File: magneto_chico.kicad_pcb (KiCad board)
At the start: 2 copper layers, 53 parts, among them P1 CONN_01X02, P2 CONN_01X01, P3 CONN_01X01, P4 CONN_01X01, P5 CONN_5, P6 CONN_01X04, Q1 BC817-40, Q2 BC817-40, Q3 BC817-40, Q4 BC807-40, Q5 IRF540, Q6 BC817-40, SW1 SPST, U1 78L33, U2 STM32F030K6, U3 LM358

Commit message: empiezo a rutear
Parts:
- C1: footprint LOCAL_Connectors_Molex:Molex_KK_6410-03 -> LOCAL_Capacitors_ThroughHole:C_Radial_D10_L20_P5
- C5, C6, C7, Q1, Q2, Q3, Q4, Q6, R1, R10, R11, R12, R13, R14, R15, R16, R17, R2, R20, R3, R4, R5, R6, R7, R8, R9, U2, U3: moved to B.Cu
- SP1: footprint LOCAL_Pin_Headers:Pin_Header_Straight_1x02 -> LOCAL_Capacitors_ThroughHole:C_Radial_D10_L20_P5
- moved R2 121.9 mm to (115.6, 72.4), turned to 270 degrees
- moved Q1 121.2 mm to (112.5, 72.4), turned to 180 degrees
- moved P1 119.8 mm to (103.1, 65.3), turned to 180 degrees
- moved C4 119.0 mm to (127.8, 65.0), turned to 90 degrees
- moved U1 116.8 mm to (103.4, 80.5), turned to 90 degrees
- moved R1 112.8 mm to (119.9, 80.5), turned to 90 degrees
- moved C3 111.8 mm to (108.7, 81.8), turned to 90 degrees
- moved C1 108.3 mm to (115.8, 68.1), turned to 90 degrees
- moved P3 107.5 mm to (114.3, 81.8)
- moved C2 104.4 mm to (103.1, 91.7), turned to 180 degrees
- moved R3 103.8 mm to (153.4, 74.4)
- moved P4 99.2 mm to (127.8, 72.6)
- moved P2 97.5 mm to (110.7, 92.7)
- moved C5 97.3 mm to (153.7, 77.2)
- moved D1 97.3 mm to (108.0, 75.4), turned to 90 degrees
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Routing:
- net GND: track 0.00 -> 229.2 mm
- net /Sheet56FC57FC/V3.3: track 0.00 -> 46.7 mm
- net Net-(C1-Pad1): track 0.00 -> 39.9 mm
- net Net-(D7-Pad2): track 0.00 -> 34.9 mm
- net Net-(D7-Pad1): track 0.00 -> 30.9 mm
- net Net-(D6-Pad2): track 0.00 -> 29.8 mm
- net /Sheet56FC57FC/V12_MOSFET: track 0.00 -> 26.5 mm
- net Net-(P5-Pad4): track 0.00 -> 16.5 mm
- net Net-(Q5-PadS): track 0.00 -> 16.2 mm
- net /Sheet56FC57FC/V5: track 0.00 -> 14.4 mm
- net Net-(R13-Pad1): track 0.00 -> 10.7 mm
- net Net-(D3-Pad1): track 0.00 -> 10.1 mm
- net Net-(R14-Pad2): track 0.00 -> 9.97 mm
- net Net-(R13-Pad2): track 0.00 -> 9.52 mm
- net Net-(P5-Pad5): track 0.00 -> 7.24 mm
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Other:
- board outline added: 105 x 80 mm

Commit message: mas pistas pero sin micro
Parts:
- moved R20 129.0 mm to (131.8, 83.3)
- moved R10 124.2 mm to (143.3, 73.7)
- moved R9 120.0 mm to (143.3, 75.9)
- moved D5 115.6 mm to (137.7, 106.9), turned to 90 degrees
- moved R12 110.4 mm to (149.1, 82.5), turned to 180 degrees
- moved R11 109.0 mm to (149.1, 78.7), turned to 180 degrees
- moved R6 108.8 mm to (137.7, 100.1), turned to 270 degrees
- moved SP1 108.4 mm to (134.6, 79.0), turned to 90 degrees
- moved Q6 108.1 mm to (131.6, 80.3), turned to 180 degrees
- moved C6 104.1 mm to (156.2, 98.3), turned to 270 degrees
- moved Q4 95.5 mm to (155.2, 84.3), turned to 270 degrees
- moved R17 93.6 mm to (162.6, 87.6)
- moved R5 93.1 mm to (143.0, 100.1), turned to 90 degrees
- moved SW1 92.5 mm to (132.3, 104.4)
- moved C8 91.0 mm to (154.2, 74.2), turned to 90 degrees
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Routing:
- net GND: track 229.2 -> 350.8 mm
- net /Sheet56FC57FC/V12_MOSFET: track 26.5 -> 56.2 mm
- net Net-(R13-Pad2): track 9.52 -> 31.8 mm
- net Net-(Q2-Pad3): track 0.00 -> 18.1 mm
- net Net-(Q3-Pad2): track 0.00 -> 17.7 mm
- net Net-(Q3-Pad1): track 0.00 -> 6.50 mm
- net Net-(Q4-Pad1): track 0.00 -> 6.09 mm
- net Net-(Q2-Pad1): track 0.00 -> 2.93 mm
- net Net-(Q5-PadS): track 16.2 -> 18.7 mm
- net Net-(R14-Pad2): track 9.97 -> 10.6 mm
- net Net-(R13-Pad1): track 10.7 -> 10.1 mm
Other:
- board size 105 x 80 mm -> 105 x 50 mm

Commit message: mas routeado casi terminado
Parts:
- R1: footprint Resistors_SMD:R_0805_HandSoldering -> Resistors_ThroughHole:Resistor_Horizontal_RM7mm; moved to F.Cu
- moved D2 21.1 mm to (109.9, 107.4), turned to 90 degrees
- moved C2 19.9 mm to (119.1, 103.5), turned to 90 degrees
- moved P2 13.2 mm to (114.0, 105.5)
- moved SP1 11.5 mm to (123.3, 76.8), turned to 270 degrees
- moved R9 8.84 mm to (146.1, 84.3), turned to 90 degrees
- moved R1 8.67 mm to (118.2, 89.0)
- moved C6 7.15 mm to (154.2, 105.2), turned to 90 degrees
- moved SW1 5.74 mm to (135.0, 99.3), turned to 270 degrees
- moved R7 4.77 mm to (143.6, 68.3), turned to 270 degrees
- moved C5 4.57 mm to (127.5, 89.9), turned to 90 degrees
- moved U3 4.49 mm to (159.9, 102.7)
- moved D4 4.20 mm to (142.7, 102.7)
- moved D5 4.19 mm to (137.7, 102.7)
- moved R3 3.75 mm to (130.6, 89.9), turned to 90 degrees
- moved R10 3.02 mm to (142.5, 76.6)
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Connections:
- U2 pad 19: Net-(R6-Pad1) -> Net-(U2-Pad19)
- U2 pad 20: Net-(R5-Pad1) -> Net-(U2-Pad20)
- U2 pad 21: Net-(R20-Pad2) -> Net-(U2-Pad21)
- U2 pad 22: Net-(SW1-Pad1) -> Net-(U2-Pad22)
- U2 pad 26: Net-(U2-Pad26) -> Net-(R5-Pad1)
- U2 pad 28: Net-(U2-Pad28) -> Net-(R6-Pad1)
- U2 pad 30: Net-(U2-Pad30) -> Net-(SW1-Pad1)
- U2 pad 8: Net-(U2-Pad8) -> Net-(R20-Pad2)
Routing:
- net /Sheet56FC57FC/V5: track 14.4 -> 78.4 mm, vias 0 -> 4
- net GND: track 350.8 -> 409.2 mm
- net /Sheet56FC57FC/V3.3: track 46.7 -> 88.5 mm, vias 0 -> 2
- net Net-(C7-Pad2): track 0.00 -> 27.7 mm
- net /Sheet56FC57FC/V12_MOSFET: track 56.2 -> 67.2 mm, vias 0 -> 2
- net Net-(Q2-Pad1): track 2.93 -> 13.3 mm
- net Net-(D6-Pad1): track 0.00 -> 9.40 mm
- net Net-(R5-Pad1): track 0.00 -> 8.75 mm
- net /Sheet56FC57FC/V3.3_ANALOG: track 0.00 -> 8.58 mm
- net Net-(Q6-Pad3): track 0.00 -> 7.95 mm
- net Net-(Q2-Pad3): track 18.1 -> 10.2 mm
- net Net-(R13-Pad2): track 31.8 -> 39.2 mm, vias 0 -> 2
- net Net-(SW1-Pad1): track 0.00 -> 7.45 mm
- net Net-(C6-Pad2): track 0.00 -> 7.19 mm
- net Net-(R6-Pad1): track 0.00 -> 6.44 mm
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
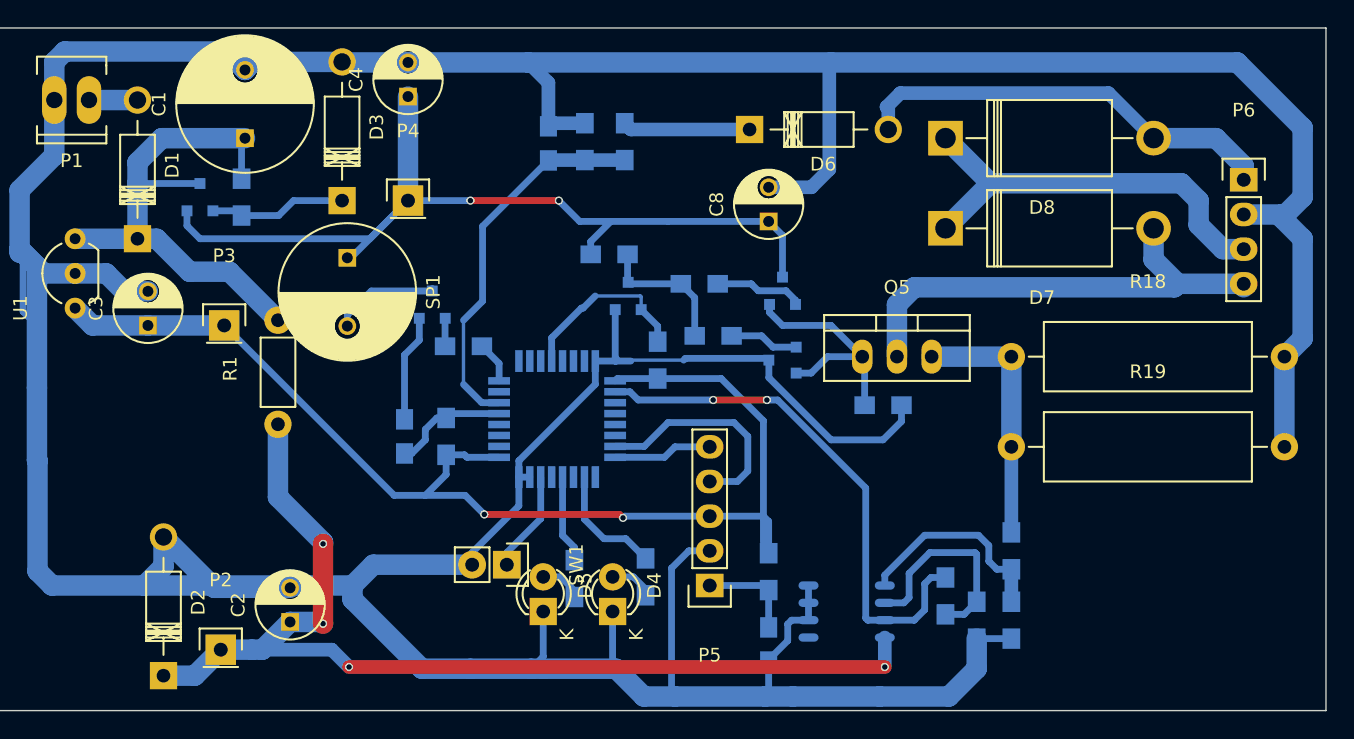
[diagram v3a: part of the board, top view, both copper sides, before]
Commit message: mejor ruteo, faltan 3 pistas
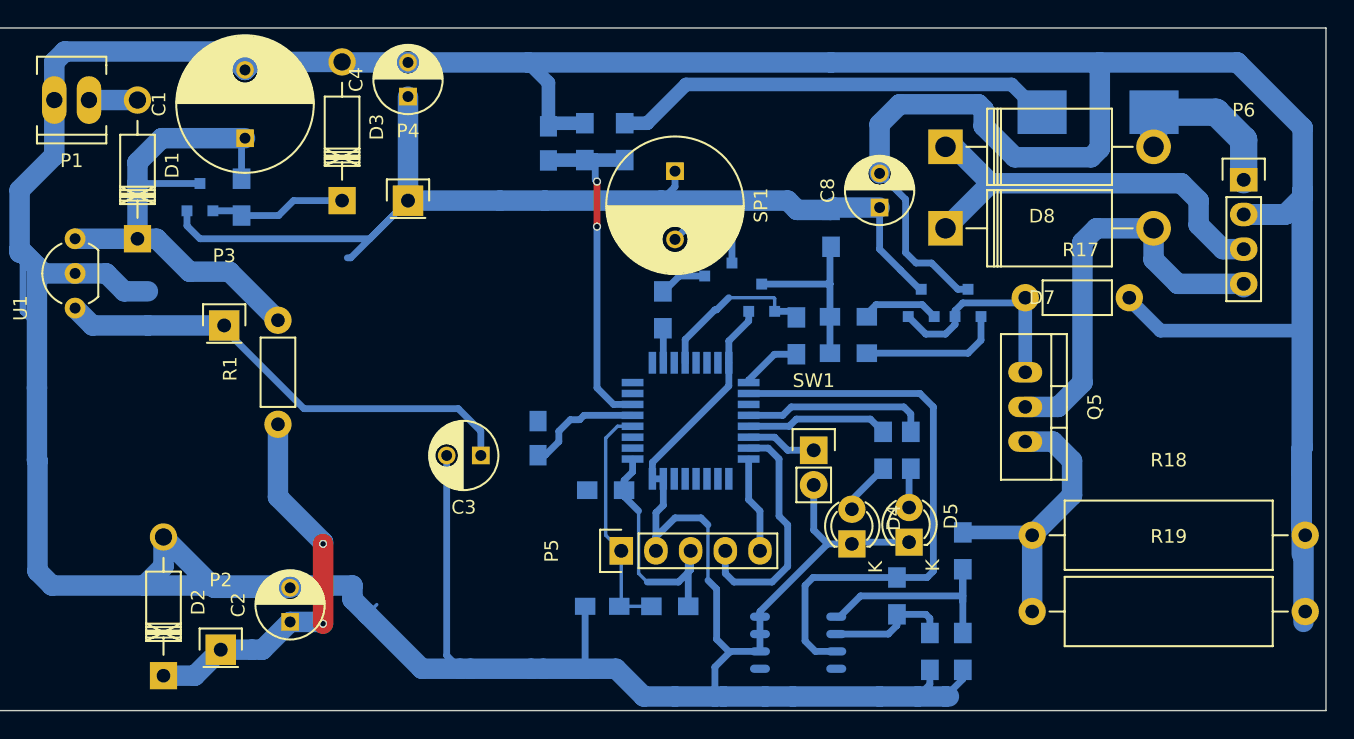
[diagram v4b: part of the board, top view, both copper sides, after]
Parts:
- D6: footprint LOCAL_Diode_ThroughHole:Diode_DO-41_SOD81_Horizontal_RM10 -> Diodes_SMD:DO-214AB_Handsoldering; moved to B.Cu
- R17: footprint Resistors_SMD:R_0805_HandSoldering -> Resistors_ThroughHole:Resistor_Horizontal_RM7mm; moved to F.Cu
- moved D5 27.3 mm to (164.5, 97.7)
- moved R6 26.4 mm to (164.6, 90.9)
- moved C3 26.2 mm to (133.1, 91.3), turned to 180 degrees
- moved D6 25.6 mm to (178.3, 66.2)
- moved SP1 24.8 mm to (147.3, 70.5)
- moved SW1 24.0 mm to (157.5, 90.9), turned to 0 degrees
- moved Q6 21.2 mm to (150.5, 77.2), turned to 90 degrees
- moved R5 19.7 mm to (162.6, 90.9)
- moved D4 18.2 mm to (160.3, 97.8)
- moved R10 16.4 mm to (158.8, 74.7), turned to 270 degrees
- moved R20 14.8 mm to (146.4, 80.6), turned to 90 degrees
- moved Q4 14.2 mm to (168.8, 80.1), turned to 180 degrees
- moved R18 13.2 mm to (173.5, 97.2)
- moved R17 13.1 mm to (173.0, 79.8)
- moved C6 12.5 mm to (142.0, 102.4), turned to 0 degrees
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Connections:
- R20 pad 1: Net-(Q6-Pad1) -> Net-(R20-Pad1)
- R20 pad 2: Net-(R20-Pad2) -> Net-(Q6-Pad1)
- U2 pad 10: Net-(U2-Pad10) -> Net-(R20-Pad1)
- U2 pad 20: Net-(U2-Pad20) -> Net-(R6-Pad1)
- U2 pad 21: Net-(U2-Pad21) -> Net-(R5-Pad1)
- U2 pad 22: Net-(U2-Pad22) -> Net-(SW1-Pad1)
- U2 pad 26: Net-(R5-Pad1) -> Net-(U2-Pad26)
- U2 pad 28: Net-(R6-Pad1) -> Net-(U2-Pad28)
- U2 pad 30: Net-(SW1-Pad1) -> Net-(U2-Pad30)
- U2 pad 8: Net-(R20-Pad2) -> Net-(U2-Pad8)
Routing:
- net GND: track 409.2 -> 478.0 mm
- net /Sheet56FC57FC/V5: track 78.4 -> 29.3 mm, vias 4 -> 2
- net /Sheet56FC57FC/V3.3: track 88.5 -> 60.4 mm, vias 2 -> 0
- net Net-(D6-Pad1): track 9.40 -> 32.7 mm
- net Net-(D6-Pad2): track 31.5 -> 14.8 mm
- net /Sheet56FC57FC/V12_MOSFET: track 67.2 -> 79.7 mm, vias 2 -> 0
- net Net-(C6-Pad2): track 7.19 -> 17.5 mm
- net Net-(R6-Pad1): track 6.44 -> 13.7 mm
- net Net-(R13-Pad1): track 15.5 -> 9.12 mm
- net Net-(Q4-Pad1): track 5.07 -> 10.5 mm
- net Net-(D7-Pad2): track 34.9 -> 30.7 mm
- net Net-(R13-Pad2): track 39.2 -> 42.6 mm, vias 2 -> 0
- net Net-(Q2-Pad3): track 10.2 -> 13.4 mm
- net Net-(R20-Pad2): track 3.06 -> 0.00 mm
- net Net-(Q5-PadS): track 18.7 -> 21.4 mm
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
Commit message: todo ruteado y pasa DRC
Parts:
- removed P2: CONN_01X01, LOCAL_Pin_Headers:Pin_Header_Straight_1x01
- added REF**: MountingHole_3.2mm_M3, Mounting_Holes:MountingHole_3.2mm_M3, F.Cu at (192.5, 62.4)
- added REF**: MountingHole_3.2mm_M3, Mounting_Holes:MountingHole_3.2mm_M3, F.Cu at (191.0, 106.8)
- added REF**: MountingHole_3.2mm_M3, Mounting_Holes:MountingHole_3.2mm_M3, F.Cu at (117.9, 106.9)
- D3: footprint LOCAL_Diode_ThroughHole:Diode_DO-41_SOD81_Horizontal_RM10 -> Diodes_SMD:MELF_Handsoldering; moved to B.Cu
- moved D2 55.9 mm to (165.7, 106.0), turned to 0 degrees
- moved C2 42.9 mm to (161.9, 105.8), turned to 270 degrees
- moved R1 37.3 mm to (151.0, 106.8), turned to 180 degrees
- moved Q1 26.2 mm to (138.3, 67.6), turned to 270 degrees
- moved U1 25.7 mm to (129.0, 80.9)
- moved D1 21.3 mm to (129.0, 72.5), turned to 180 degrees
- moved R2 20.1 mm to (135.4, 68.8)
- moved P3 19.5 mm to (133.7, 80.9)
- moved C4 19.4 mm to (147.2, 65.0)
- moved C3 15.6 mm to (135.0, 75.8)
- moved P1 14.6 mm to (117.7, 65.5)
- moved C7 14.4 mm to (152.4, 67.3)
- moved R7 14.4 mm to (158.0, 67.3)
- moved R8 14.4 mm to (155.1, 67.3)
- moved C1 11.4 mm to (127.3, 67.6)
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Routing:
- net GND: track 478.0 -> 452.5 mm
- net Net-(C1-Pad1): track 39.2 -> 64.1 mm
- net /Sheet56FC57FC/V3.3: track 60.4 -> 83.3 mm, vias 0 -> 4
- net /Sheet56FC57FC/V12_MOSFET: track 79.7 -> 60.3 mm
- net Net-(C7-Pad2): track 25.4 -> 41.3 mm
- net Net-(D6-Pad1): track 32.7 -> 17.8 mm
- net /Sheet56FC57FC/V5: track 29.3 -> 16.6 mm, vias 2 -> 0
- net Net-(Q6-Pad1): track 3.53 -> 13.9 mm
- net Net-(D1-Pad2): track 3.55 -> 7.04 mm
- net Net-(Q6-Pad3): track 6.73 -> 4.24 mm
- net /Sheet56FC57FC/V3.3_ANALOG: track 8.58 -> 10.6 mm
- net Net-(R13-Pad2): track 42.6 -> 40.8 mm
- net Net-(Q2-Pad1): track 12.3 -> 13.7 mm
- net Net-(R13-Pad1): track 9.12 -> 10.3 mm
- net Net-(R14-Pad2): track 17.1 -> 16.1 mm
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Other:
- board size 105 x 50 mm -> 81 x 50 mm

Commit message: todo termiando con plano de masa y pines .2
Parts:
- P6: footprint LOCAL_Pin_Headers:Pin_Header_Straight_1x04 -> LOCAL_Connect:bornier4
- moved P6 6.15 mm to (189.5, 77.2), turned to 270 degrees
- renumbered REF** to ?
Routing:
- net GND: track 452.5 -> 426.7 mm
- net Net-(D7-Pad2): track 30.7 -> 36.0 mm
- net Net-(D7-Pad1): track 30.7 -> 34.6 mm
- net Net-(D6-Pad2): track 14.8 -> 12.0 mm
- net Net-(C7-Pad2): track 41.3 -> 39.6 mm
- added copper zone on B.Cu, net GND
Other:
- net class Default: via_dia 0.6 -> 1.2; via_drill 0.4 -> 0.8
- rule via_min_drill: 0.3 -> 0.8
- rule via_min_size: 0.4 -> 1.2
